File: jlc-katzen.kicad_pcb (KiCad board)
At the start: 4 copper layers, 59.4 x 52.2 mm, 62 parts, among them J1 USB_C_Receptacle_USB2.0_16P, J2 Conn_01x04, J3 Conn_01x04, J4 Conn_01x02, J5 Conn_ARM_SWD_TagConnect_TC2030, Q1 2N7002, Q2 2N7002, Q3 2N7002, U1 XC6206P332MR, U2 W25Q128JVSIQ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

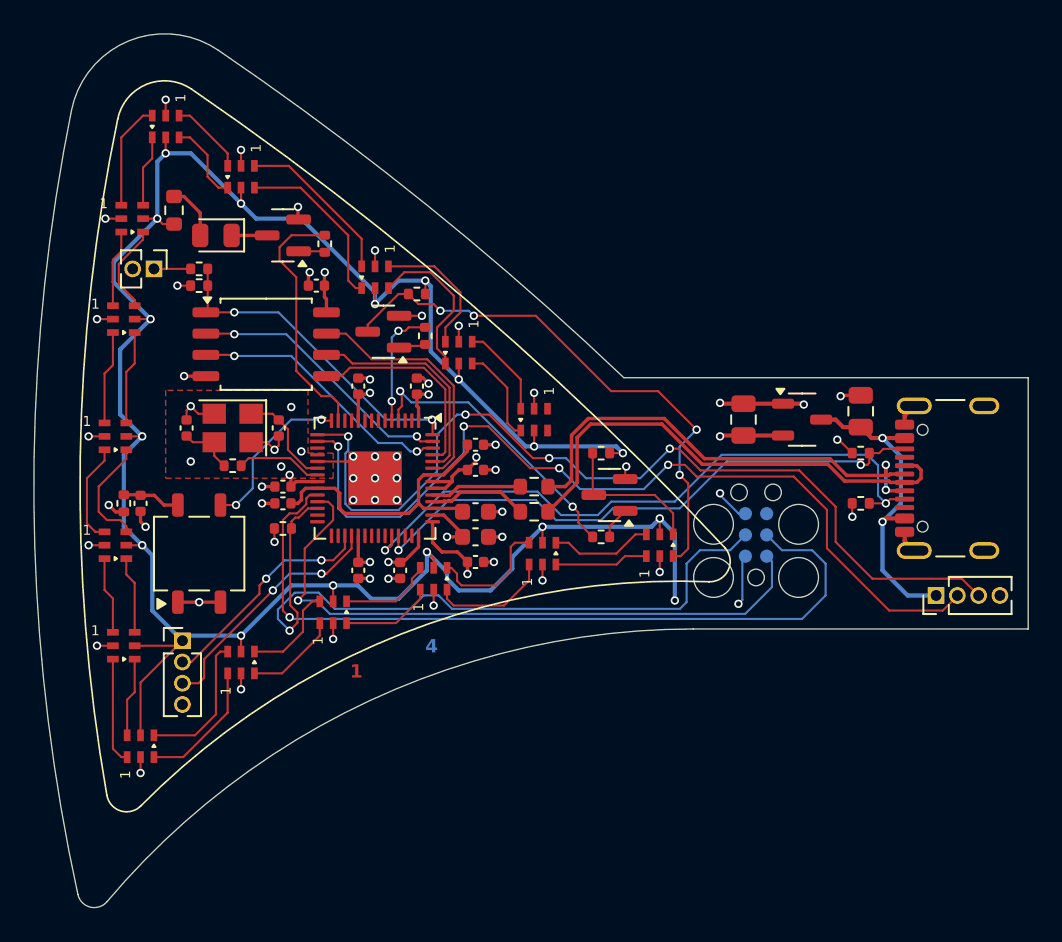
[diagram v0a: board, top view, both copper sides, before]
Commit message: clean silk, tweak traces more
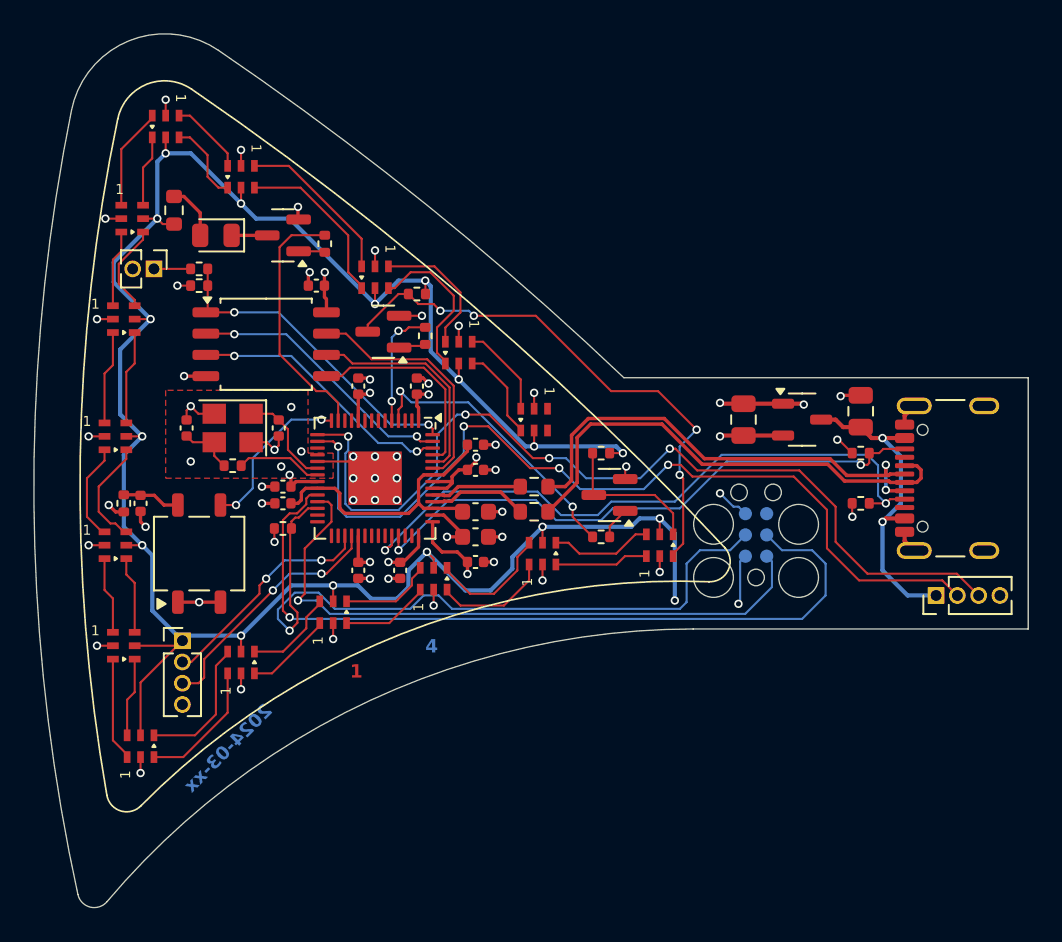
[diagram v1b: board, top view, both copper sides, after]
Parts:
- D2: value LED -> IR LED
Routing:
- net /PAIR_IN_RX: track 52.9 -> 52.1 mm
- net +5V: track 176.1 -> 175.4 mm
- net /LED_DAT_5V: track 33.0 -> 32.5 mm
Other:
- board text added: "2024-03-xx"

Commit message: more silk, tweaks
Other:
- board text added: "+V"
- board text added: "BOOT"
- board text added: "GND"
- board text added: "SWC"
- board text added: "SWD"
- board text added: "~{RST}"

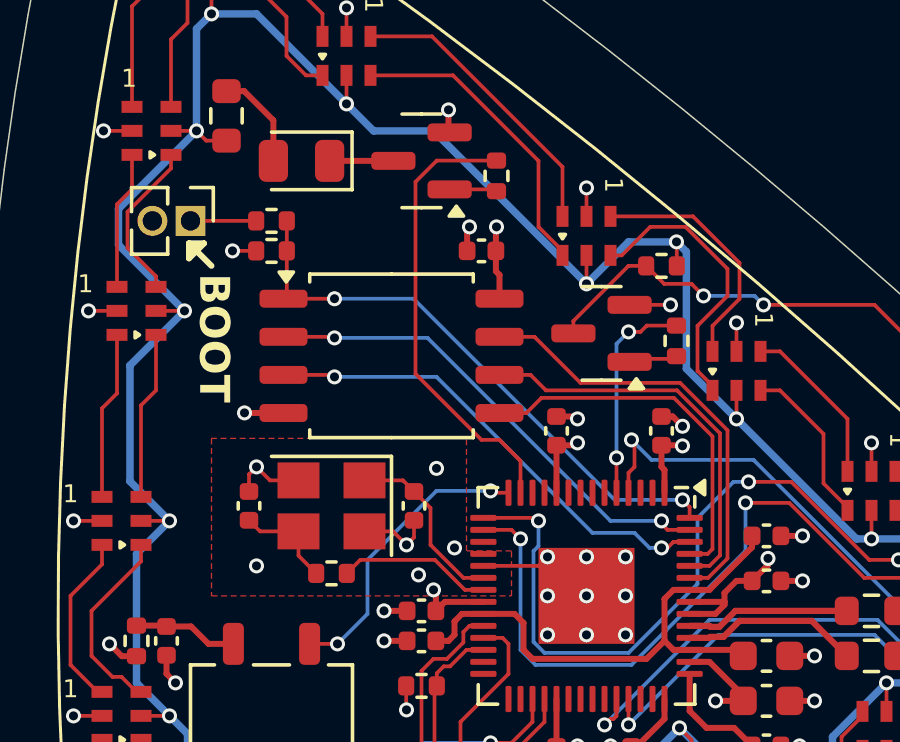
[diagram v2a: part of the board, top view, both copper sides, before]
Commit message: move ir tx/rx to separate pwm blocks
(even if we use PIO instead)
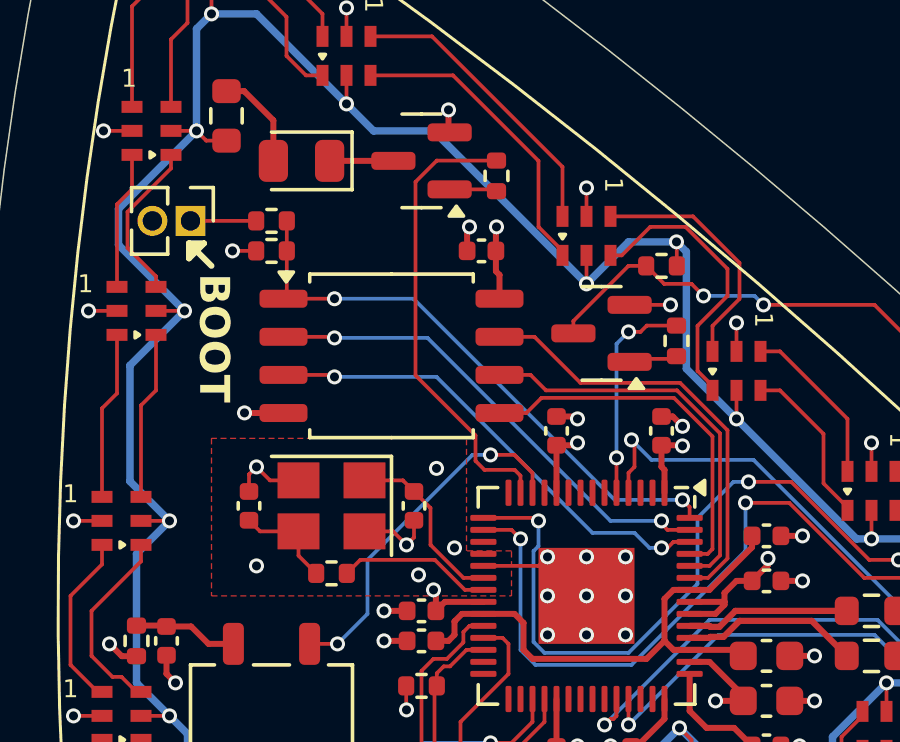
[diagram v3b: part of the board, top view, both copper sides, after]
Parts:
- D2: value IR LED -> LED
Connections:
- U3 pad 12: unconnected-(U3-GPIO9-Pad12) -> /IR_RX
- U3 pad 14: /IR_RX -> unconnected-(U3-GPIO11-Pad14)
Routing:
- net /IR_RX: track 9.82 -> 12.0 mm
